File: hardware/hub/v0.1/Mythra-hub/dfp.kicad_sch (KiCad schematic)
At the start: 22 parts, among them J3 918-418K2022C40000, U4 HD3SS460, U8 SiC437/8

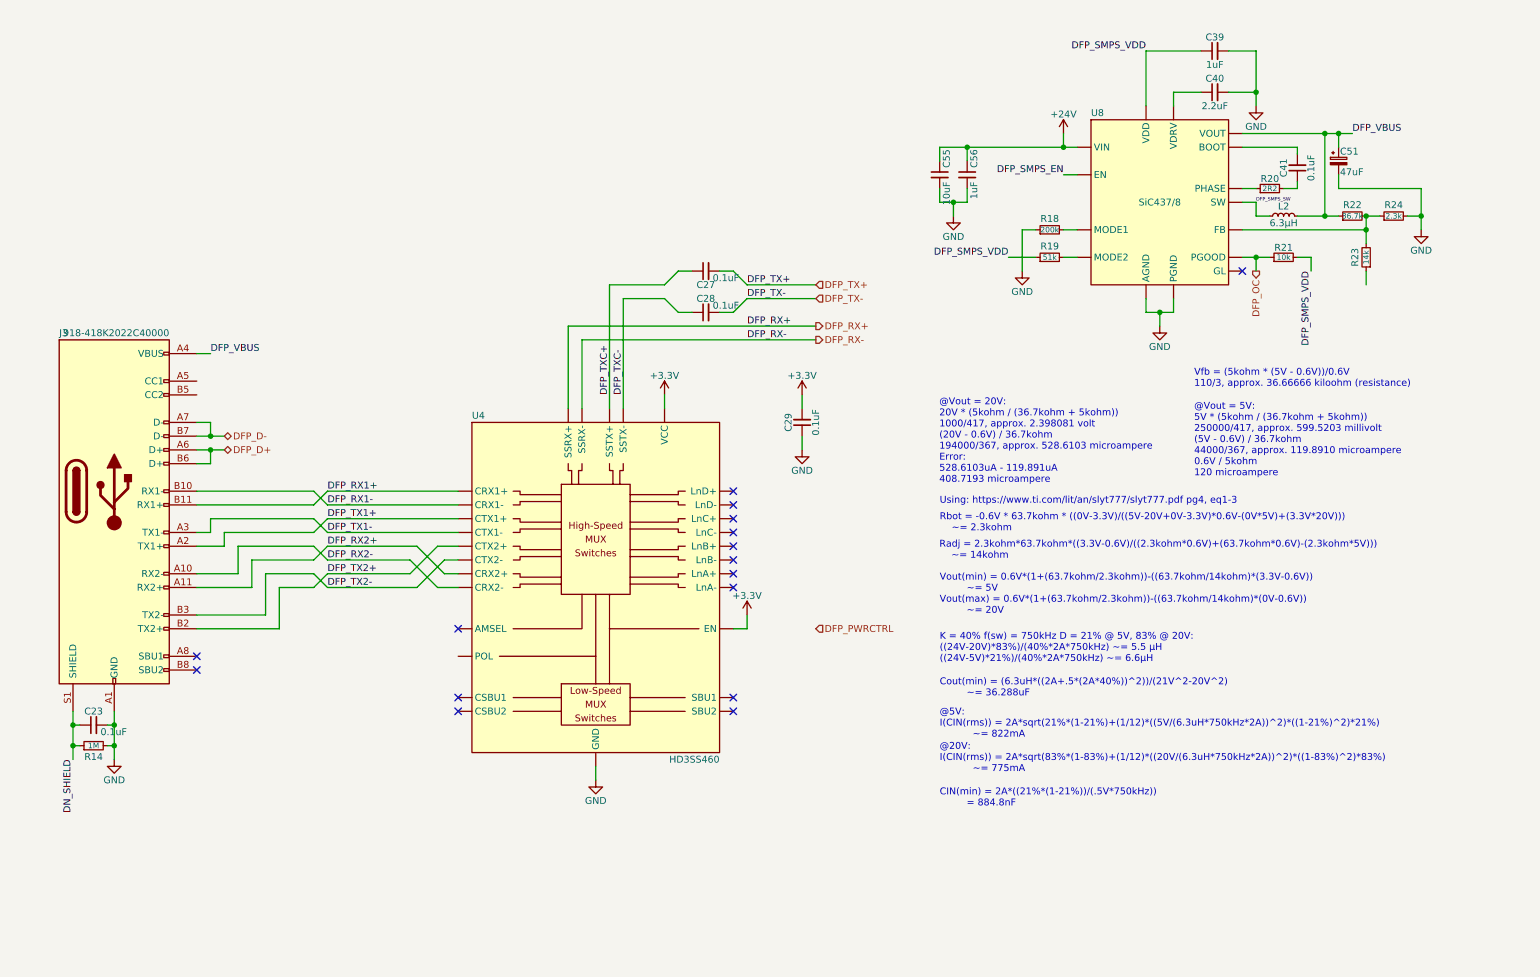
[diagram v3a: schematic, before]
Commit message: Added power delivery control to the DFPs
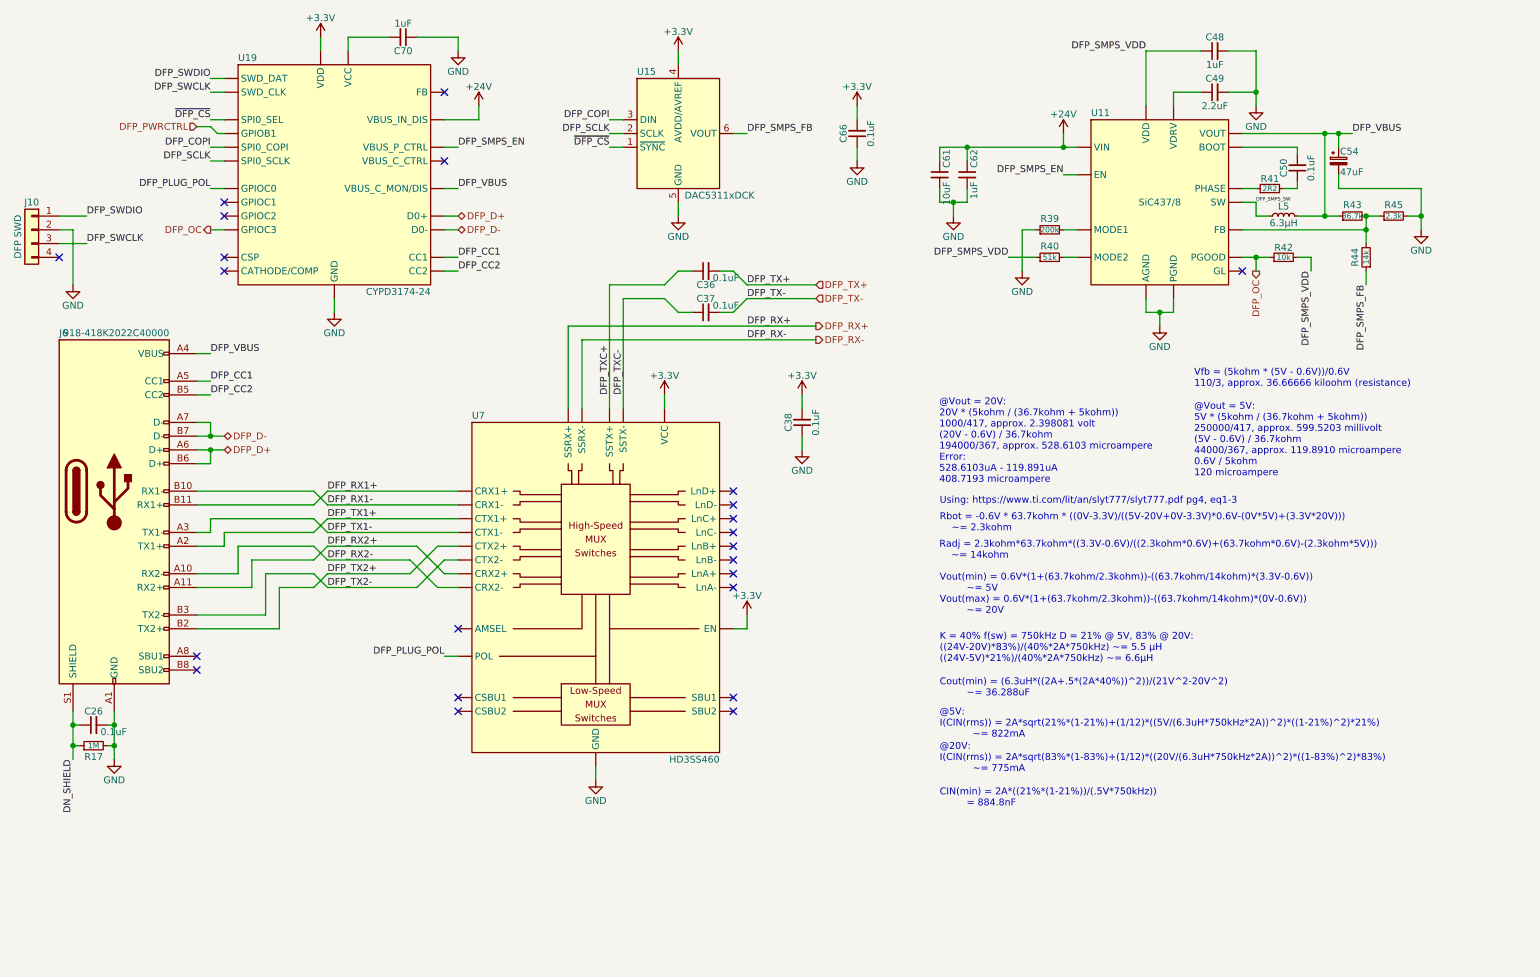
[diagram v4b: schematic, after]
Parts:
- added C66: 0.1uF, rhais_rcl:C0402, symbol Device:C_Small
- added C70: 1uF, rhais_rcl:C0402, symbol Device:C_Small
- added J10: DFP SWD, rhais_connector-pinheader:PinHeader_1x04_P1.27mm_Vertical, symbol Connector_Generic:Conn_01x04
- added U15: DAC5311xDCK, rhais_package-smd:SOT-363_SC-70-6, symbol Analog_DAC:DAC5311xDCK
- added U19: CYPD3174-24, rhais_package-qfn:QFN-24-1EP_4x4mm_P0.5mm_EP2.6x2.6mm, symbol DX-MON:CYPD3174-24
- renumbered C23 to C26, C27 to C36, C28 to C37, C29 to C38, C39 to C48, C40 to C49, C41 to C50, C51 to C54, C55 to C61, C56 to C62, J3 to J6, L2 to L5, R14 to R17, R18 to R39, R19 to R40, R20 to R41, R21 to R42, R22 to R43, R23 to R44, R24 to R45, U8 to U11, U4 to U7
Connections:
- net +24V: now also U19.18 (VBUS_IN_DIS)
- net +3V3: now also C66.2, U15.4 (AVDD/AVREF), U19.23 (VDD)
- net DFP_D+: now also U19.17 (GPIOD0)
- net DFP_D-: now also U19.16 (GPIOD1)
- net DFP_OC: now also U19.13 (GPIOC3)
- net DFP_PWRCTRL: now also U19.2 (GPIOB1)
- net DFP_SMPS_EN: now also U19.3 (VBUS_P_CTRL)
- net DFP_VBUS: now also U19.11 (VBUS_C_MON/DIS)
- net GND: now also C66.1, C70.1, J10.2 (Pin_2), U15.5 (GND), U19.15 (GND), U19.25 (GND)
- net DFP_CC1: now reaches J6.A5 (CC1)
- net DFP_CC1: now also U19.15 (GND)
- net DFP_CC2: now reaches J6.B5 (CC2)
- net DFP_CC2: now also U19.14 (CC2)
- net DFP_PLUG_POL: now reaches U7.3 (POL)
- net DFP_PLUG_POL: now also U19.9 (GPIOC0)
- net DFP_SMPS_FB: now reaches R44.1
- net DFP_SMPS_FB: now also U15.6 (VOUT)
- new net: C70.2, U19.24 (VCC)
- new net DFP_COPI: U15.3 (DIN), U19.5 (GPIOB2)
- new net DFP_SCLK: U15.2 (SCLK), U19.6 (GPIOB3)
- new net DFP_SWCLK: J10.3 (Pin_3), U19.8 (GPIOA1)
- new net DFP_SWDIO: J10.1 (Pin_1), U19.7 (GPIOA0)
- new net ~{DFP_CS}: U15.1 (~{SYNC}), U19.1 (GPIOB0)
- no-connect marks 16 -> 23

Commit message: Fixed some ERC errors
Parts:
- renumbered C26 to C23, C36 to C27, C37 to C28, C38 to C29, C48 to C39, C49 to C40, C50 to C41, C54 to C51, C61 to C55, C62 to C56, C66 to C63, C70 to C67, J6 to J3, J10 to J7, L5 to L2, R17 to R14, R39 to R18, R40 to R19, R41 to R20, R42 to R21, R43 to R22, R44 to R23, R45 to R24, U15 to U12, U19 to U16, U7 to U4, U11 to U8

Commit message: Version controlled the changes from the last stream, including the addition of the 3.3V DC-DC, config I2C EEPROM and test points
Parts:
- added C76: 0.1uF, rhais_rcl:C0402, symbol Device:C_Small
- added TP8: VBUS, TestPoint:TestPoint_Pad_D1.0mm, symbol Connector:TestPoint
- C26: renamed from C23; MFR (none) -> Yageo; MPN (none) -> RC0402FR-0710KL; OC_LCSC (none) -> C60490; URL_LCSC (none) -> https://www.lcsc.com/product-detail/Chip-Resistor-Surface-M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
- C36: renamed from C27; MFR (none) -> Yageo; MPN (none) -> RC0402FR-0710KL; OC_LCSC (none) -> C60490; URL_LCSC (none) -> https://www.lcsc.com/product-detail/Chip-Resistor-Surface-M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
- C37: renamed from C28; MFR (none) -> Yageo; MPN (none) -> RC0402FR-0710KL; OC_LCSC (none) -> C60490; URL_LCSC (none) -> https://www.lcsc.com/product-detail/Chip-Resistor-Surface-M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
- C38: renamed from C29; MFR (none) -> Yageo; MPN (none) -> RC0402FR-0710KL; OC_LCSC (none) -> C60490; URL_LCSC (none) -> https://www.lcsc.com/product-detail/Chip-Resistor-Surface-M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
- C50: renamed from C41; MFR (none) -> Yageo; MPN (none) -> RC0402FR-0710KL; OC_LCSC (none) -> C60490; URL_LCSC (none) -> https://www.lcsc.com/product-detail/Chip-Resistor-Surface-M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
- C66: renamed from C63; MFR (none) -> Yageo; MPN (none) -> RC0402FR-0710KL; OC_LCSC (none) -> C60490; URL_LCSC (none) -> https://www.lcsc.com/product-detail/Chip-Resistor-Surface-M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
- J10: renamed from J7; MFR (none) -> Multicomp; MPN (none) -> MC-HVT1-S04-G; OC_FARNELL (none) -> 2852586; URL_FARNELL (none) -> https://uk.farnell.com/multicomp/mc-hvt1-s04-g/connector-he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
- R44: renamed from R23; OC_FARNELL MCWR04X1402FTL -> 2447109
- renumbered C39 to C48, C40 to C49, C51 to C54, C55 to C61, C56 to C62, C67 to C70, J3 to J6, L2 to L5, R14 to R17, R18 to R39, R19 to R40, R20 to R41, R21 to R42, R22 to R43, R24 to R45, U8 to U11, U12 to U15, U16 to U19, U4 to U7
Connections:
- net +3V3: now also C76.2
- net DFP_VBUS: now also TP8.1
- net GND: now also C76.1
- no-connect marks 23 -> 22

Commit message: Completed a first pass on the azonenburg schematic checklist and begun adding the per-port indicator LEDs that had been forgotten
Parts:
- added C86: 1nF, rhais_rcl:C0402, symbol Device:C_Small
- added C90: 47uF, rhais_rcl:C_Elec_8.3x8.3mm, symbol Device:C_Polarized_Small
- added D1: WHITE, rhais_led:LED0603, symbol Device:LED
- added D5: ICE BLUE, rhais_led:LED0603, symbol Device:LED
- added D6: PINK, rhais_led:LED0603, symbol Device:LED
- added R55, R60: 2k2, rhais_rcl:R0402, symbol Device:R_Small
- added R59: 5k5, rhais_rcl:R0402, symbol Device:R_Small
- added U23, U24: TPD4E02B04DQA, rhais_package-qfn:USON-10_2.5x1.0mm_P0.5mm, symbol DX-MON:TPD4E02B04DQA
- added U31: SP3400-02UTG, rhais_package-qfn:UDFN-6L, symbol DX-MON:SP3400-02UTG
- renumbered C26 to C23, C36 to C27, C37 to C28, C38 to C29, C48 to C39, C49 to C40, C50 to C41, C54 to C51, C61 to C55, C62 to C56, C66 to C63, C70 to C67, C76 to C73, J6 to J3, J10 to J7, L5 to L2, R17 to R14, R39 to R18, R40 to R19, R41 to R20, R42 to R21, R43 to R22, R44 to R23, R45 to R24, TP8 to TP5, U15 to U12, U19 to U16, U7 to U4, U11 to U8
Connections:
- net +24V: now also C90.1
- net DFP_D+: now also U31.2 (IO2), U31.5 (NC)
- net DFP_D-: now also U31.1 (IO1), U31.6 (NC)
- net DFP_RX1+: now also U23.1 (IO1), U23.10 (NC)
- net DFP_RX1-: now also U23.2 (IO2), U23.9 (NC)
- net DFP_RX2+: now also U24.4 (IO3), U24.7 (NC)
- net DFP_RX2-: now also U24.5 (IO4), U24.6 (NC)
- net DFP_SMPS_EN: now also R55.1
- net DFP_TX1+: now also U23.4 (IO3), U23.7 (NC)
- net DFP_TX1-: now also U23.5 (IO4), U23.6 (NC)
- net DFP_TX2+: now also U24.1 (IO1), U24.10 (NC)
- net DFP_TX2-: now also U24.2 (IO2), U24.9 (NC)
- net DN_SHIELD: now also C86.1
- net GND: now also C86.2, C90.2, D1.1 (K), D5.1 (K), D6.1 (K), U23.3 (G), U23.8 (G), U24.3 (G), U24.8 (G), U31.3 (GND), U31.4 (GND)
- net PDF_PD_OK: now reaches U16.10 (GPIOC1)
- net PDF_PD_OK: now also R59.1
- new net: D6.2 (A), R60.2
- new net: D5.2 (A), R59.2
- new net: D1.2 (A), R55.2
- no-connect marks 22 -> 21
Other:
- note added: "PD success"
- note added: "Port OC"
- note added: "Port power"
- note added: "Port speed"
- moved on the sheet: R14

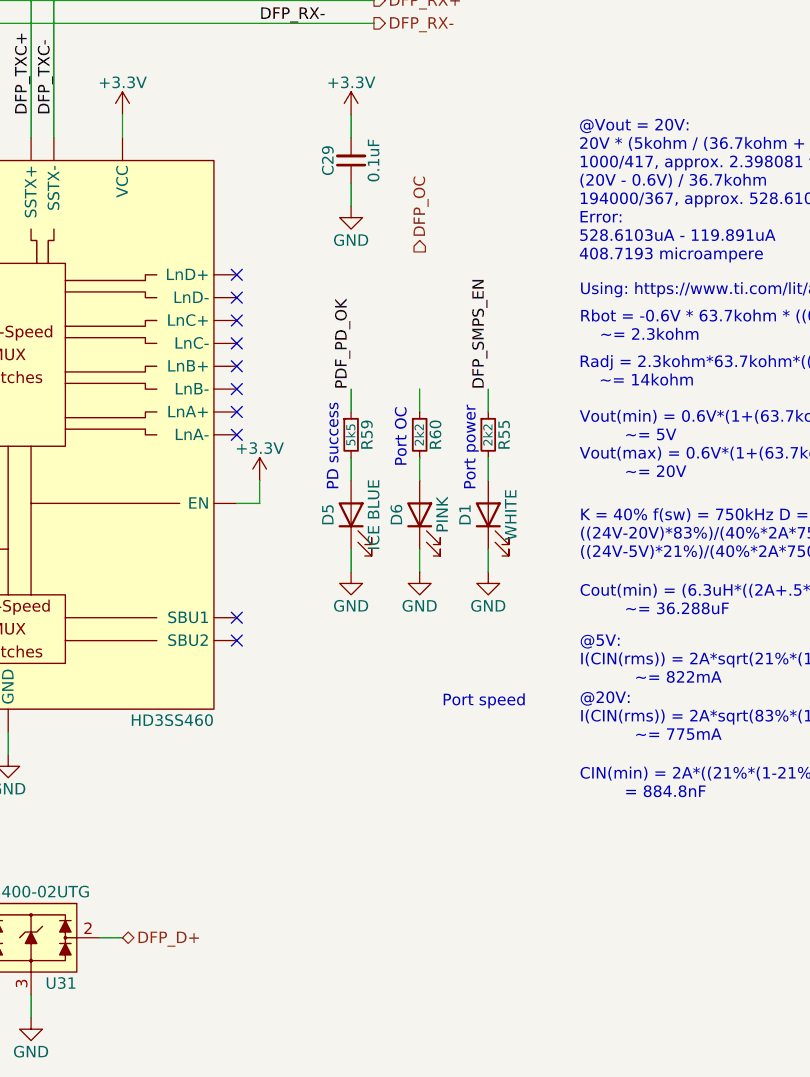
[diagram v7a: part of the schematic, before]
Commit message: More work toward per-port LED state indicators
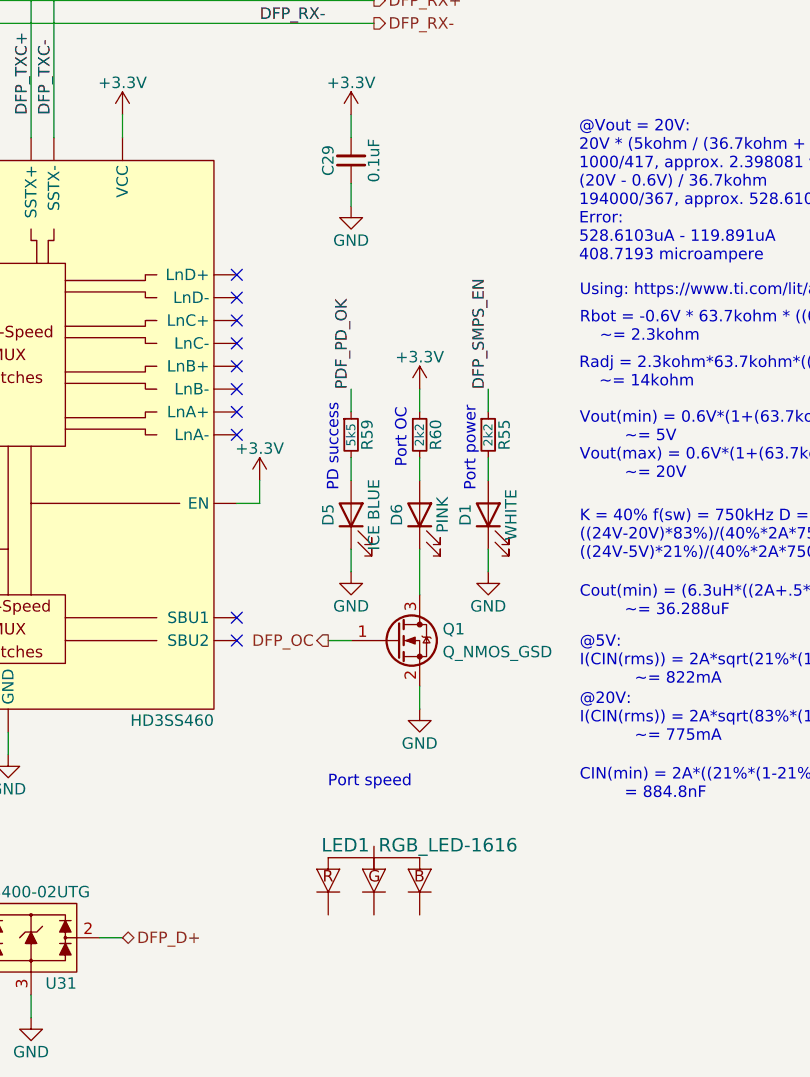
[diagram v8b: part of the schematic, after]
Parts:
- added LED1: RGB_LED-1616, rhais_led:LED0606_Clockwise, symbol DX_MON:RGB_LED-1616
- added Q1: Q_NMOS_GSD, rhais_package-smd:SOT-23, symbol Device:Q_NMOS_GSD
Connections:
- net +3V3: now also R60.1
- net DFP_OC: now also Q1.1 (G)
- net GND: now also Q1.2 (S); no longer D6.1 (K)
- new net: D6.1 (K), Q1.3 (D)
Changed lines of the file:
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@@
+    (stroke (width 0) (type default) (color 0 0 0 0))
+  )
+  (wire (pts (xy 162.56 144.78) (xy 160.02 144.78))
     (stroke (width 0) (type default) (color 0 0 0 0))
   )
@@
     (stroke (width 0) (type default) (color 0 0 0 0))
   )
-  (wire (pts (xy 170.18 137.16) (xy 170.18 134.62))
+  (wire (pts (xy 170.18 139.7) (xy 170.18 134.62))
+    (stroke (width 0) (type default) (color 0 0 0 0))
+  )
+  (wire (pts (xy 170.18 152.4) (xy 170.18 149.86))
     (stroke (width 0) (type default) (color 0 0 0 0))
   )
@@
     (stroke (width 0) (type solid) (color 0 0 0 0))
   )
+  (text "Port speed" (at 159.9752 161.2541 0)
+    (effects (font (size 1.27 1.27)) (justify left bottom))
+  )
   (text "PD success" (at 161.29 128.27 90)
     (effects (font (size 1.27 1.27)) (justify left bottom))
   )
   (text "Port OC" (at 168.8652 125.6689 90)
-    (effects (font (size 1.27 1.27)) (justify left bottom))
-  )
-  (text "Port speed" (at 172.6752 152.3641 0)
     (effects (font (size 1.27 1.27)) (justify left bottom))
   )
@@
     (effects (font (size 1.27 1.27)) (justify left))
   )
+  (hierarchical_label "DFP_OC" (shape output) (at 160.02 144.78 180)
+    (effects (font (size 1.27 1.27)) (justify right))
+  )
   (hierarchical_label "DFP_TX+" (shape input) (at 165.1 66.04 0)
     (effects (font (size 1.27 1.27)) (justify left))
@@
     (effects (font (size 1.27 1.27)) (justify left))
   )
-  (hierarchical_label "DFP_OC" (shape output) (at 170.18 101.6 90)
-    (effects (font (size 1.27 1.27)) (justify left))
-  )
   (hierarchical_label "DFP_OC" (shape output) (at 246.38 63.5 270)
     (effects (font (size 1.27 1.27)) (justify right))
@@
     )
     (property "Datasheet" "" (id 3) (at 162.56 86.36 0)
+      (effects (font (size 1.27 1.27)) hide)
+    )
+    (pin "1")
+  )
+  (symbol (lib_id "power:+3.3V") (at 170.18 116.84 0)
+    (in_bom yes) (on_board yes)
+    (property "Reference" "#PWR0184" (id 0) (at 170.18 120.65 0)
+      (effects (font (size 1.27 1.27)) hide)
+    )
+    (property "Value" "+3.3V" (id 1) (at 170.18 113.284 0))
+    (property "Footprint" "" (id 2) (at 170.18 116.84 0)
+      (effects (font (size 1.27 1.27)) hide)
+    )
+    (property "Datasheet" "" (id 3) (at 170.18 116.84 0)
       (effects (font (size 1.27 1.27)) hide)
     )
@@
     (pin "1")
   )
-  (symbol (lib_id "power:GND") (at 170.18 137.16 0)
-    (in_bom yes) (on_board yes)
-    (property "Reference" "#PWR0177" (id 0) (at 170.18 143.51 0)
-      (effects (font (size 1.27 1.27)) hide)
-    )
-    (property "Value" "GND" (id 1) (at 170.18 140.97 0))
-    (property "Footprint" "" (id 2) (at 170.18 137.16 0)
-      (effects (font (size 1.27 1.27)) hide)
-    )
-    (property "Datasheet" "" (id 3) (at 170.18 137.16 0)
+  (symbol (lib_id "power:GND") (at 170.18 152.4 0)
+    (in_bom yes) (on_board yes)
+    (property "Reference" "#PWR0177" (id 0) (at 170.18 158.75 0)
+      (effects (font (size 1.27 1.27)) hide)
+    )
+    (property "Value" "GND" (id 1) (at 170.18 156.21 0))
+    (property "Footprint" "" (id 2) (at 170.18 152.4 0)
+      (effects (font (size 1.27 1.27)) hide)
+    )
+    (property "Datasheet" "" (id 3) (at 170.18 152.4 0)
       (effects (font (size 1.27 1.27)) hide)
     )
@@
     (pin "4")
   )
+  (symbol (lib_id "DX_MON:RGB_LED-1616") (at 165.1 170.18 0)
+    (in_bom yes) (on_board yes)
+    (property "Reference" "LED1" (id 0) (at 164.592 168.402 0)
+      (effects (font (size 1.4986 1.4986)) (justify right bottom))
+    )
+    (property "Value" "RGB_LED-1616" (id 1) (at 165.608 168.402 0)
+      (effects (font (size 1.4986 1.4986)) (justify left bottom))
+    )
+    (property "Footprint" "rhais_led:LED0606_Clockwise" (id 2) (at 165.1 170.18 0)
+      (effects (font (size 1.27 1.27)) hide)
+    )
+    (property "Datasheet" "" (id 3) (at 165.1 170.18 0)
+      (effects (font (size 1.27 1.27)) hide)
+    )
+    (pin "1")
+    (pin "2")
+    (pin "3")
+    (pin "4")
+  )
+  (symbol (lib_id "Device:Q_NMOS_GSD") (at 167.64 144.78 0)
+    (in_bom yes) (on_board yes)
+    (property "Reference" "Q1" (id 0) (at 172.72 143.51 0)
+      (effects (font (size 1.27 1.27)) (justify left))
+    )
+    (property "Value" "Q_NMOS_GSD" (id 1) (at 172.72 146.05 0)
+      (effects (font (size 1.27 1.27)) (justify left))
+    )
+    (property "Footprint" "rhais_package-smd:SOT-23" (id 2) (at 172.72 142.24 0)
+      (effects (font (size 1.27 1.27)) hide)
+    )
+    (property "Datasheet" "~" (id 3) (at 167.64 144.78 0)
+      (effects (font (size 1.27 1.27)) hide)
+    )
+    (pin "1")
+    (pin "2")
+    (pin "3")
+  )
   (symbol (lib_id "DX-MON:SP3400-02UTG") (at 127 177.8 0)
